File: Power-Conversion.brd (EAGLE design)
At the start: 160 x 100 mm, 25 parts, among them Q1 SUM90P10-19L, U7 LM2678

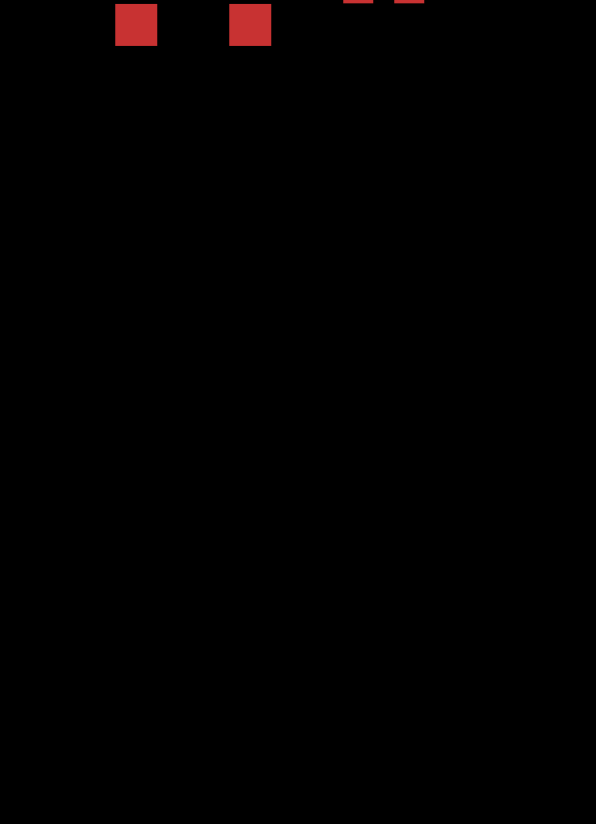
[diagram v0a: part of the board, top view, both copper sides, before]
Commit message: added current sense
added current sense and support things
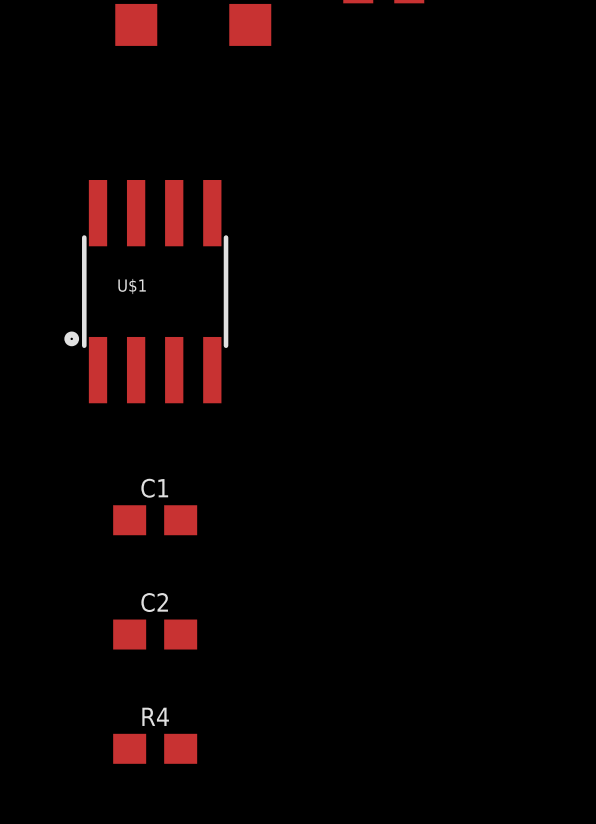
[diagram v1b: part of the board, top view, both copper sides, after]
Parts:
- added C1: .1uF, SparkFun-Capacitors:0603
- added C2: .01uF, SparkFun-Capacitors:0603
- added R4: 10k, SparkFun-Resistors:0603
- added U$1: ACS712, SparkFun-Sensors:SO08
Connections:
- new net +48_SNS: U$1.3, U$1.4
- new net 48_I_ANALOG: C2.2, R4.2, U$1.7
- net +48V: now also U$1.1, U$1.2
- net +5V: now also C1.2, U$1.8
- net GND: now also C1.1, C2.1, R4.1, U$1.5, U$1.6
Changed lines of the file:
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@@
 <attribute name="PARTNO" value="SUM90P10-19L-E3CT-ND" x="-55.88" y="-27.94" size="1.778" layer="27" display="off"/>
+</element>
+<element name="U$1" library="SparkFun-Sensors" package="SO08" value="ACS712" x="-49.53" y="-57.15">
+<attribute name="PROD_ID" value="IC-08964" x="-55.88" y="-44.45" size="1.778" layer="27" display="off"/>
+</element>
+<element name="C1" library="SparkFun-Capacitors" package="0603" value=".1uF" x="-49.53" y="-64.77">
+<attribute name="PROD_ID" value="CAP-08280" x="-55.88" y="-53.34" size="1.778" layer="27" display="off"/>
+</element>
+<element name="C2" library="SparkFun-Capacitors" package="0603" value=".01uF" x="-49.53" y="-68.58">
+<attribute name="PROD_ID" value="CAP-08280" x="-55.88" y="-57.15" size="1.778" layer="27" display="off"/>
+</element>
+<element name="R4" library="SparkFun-Resistors" package="0603" value="10k" x="-49.53" y="-72.39">
+<attribute name="PROD_ID" value="RES-00824" x="-55.88" y="-60.96" size="1.778" layer="27" display="off"/>
 </element>
 </elements>
@@
 <contactref element="LED3" pad="C"/>
 <contactref element="LED4" pad="C"/>
-<wire x1="-26.67" y1="59.17" x2="-22.86" y2="59.17" width="0" layer="19" extent="1-1"/>
-<wire x1="-15.83" y1="46.99" x2="-22.86" y2="59.17" width="0" layer="19" extent="1-1"/>
-<wire x1="-15.83" y1="40.64" x2="-15.83" y2="46.99" width="0" layer="19" extent="1-1"/>
-<wire x1="-15.83" y1="34.29" x2="-15.83" y2="40.64" width="0" layer="19" extent="1-1"/>
-<wire x1="-27.26" y1="40.64" x2="-15.83" y2="40.64" width="0" layer="19" extent="1-1"/>
-<wire x1="-27.26" y1="34.29" x2="-27.26" y2="40.64" width="0" layer="19" extent="1-1"/>
-<wire x1="-25.13" y1="26.415" x2="-27.26" y2="34.29" width="0" layer="19" extent="1-1"/>
-<wire x1="-25.13" y1="21.845" x2="-25.13" y2="26.415" width="0" layer="19" extent="1-1"/>
+<contactref element="U$1" pad="5"/>
+<contactref element="U$1" pad="6"/>
+<contactref element="C1" pad="1"/>
+<contactref element="C2" pad="1"/>
+<contactref element="R4" pad="1"/>
+<wire x1="-50.38" y1="-68.58" x2="-50.38" y2="-72.39" width="0" layer="19" extent="1-1"/>
+<wire x1="-50.38" y1="-64.77" x2="-50.38" y2="-68.58" width="0" layer="19" extent="1-1"/>
+<wire x1="-48.895" y1="-54.5338" x2="-50.38" y2="-64.77" width="0" layer="19" extent="1-1"/>
+<wire x1="-47.625" y1="-54.5338" x2="-48.895" y2="-54.5338" width="0" layer="19" extent="1-1"/>
+<wire x1="-35.56" y1="6.35" x2="-47.625" y2="-54.5338" width="0" layer="19" extent="1-1"/>
+<wire x1="-27.2288" y1="6.35" x2="-35.56" y2="6.35" width="0" layer="19" extent="1-1"/>
+<wire x1="-25.13" y1="21.845" x2="-27.2288" y2="6.35" width="0" layer="19" extent="1-1"/>
+<wire x1="-25.13" y1="26.415" x2="-25.13" y2="21.845" width="0" layer="19" extent="1-1"/>
+<wire x1="-27.26" y1="34.29" x2="-25.13" y2="26.415" width="0" layer="19" extent="1-1"/>
+<wire x1="-27.26" y1="40.64" x2="-27.26" y2="34.29" width="0" layer="19" extent="1-1"/>
 <wire x1="-35.98" y1="46.99" x2="-27.26" y2="40.64" width="0" layer="19" extent="1-1"/>
 <wire x1="-38.69" y1="40.64" x2="-35.98" y2="46.99" width="0" layer="19" extent="1-1"/>
 <wire x1="-38.69" y1="34.29" x2="-38.69" y2="40.64" width="0" layer="19" extent="1-1"/>
-<wire x1="-27.2288" y1="6.35" x2="-25.13" y2="21.845" width="0" layer="19" extent="1-1"/>
-<wire x1="-35.56" y1="6.35" x2="-27.2288" y2="6.35" width="0" layer="19" extent="1-1"/>
+<wire x1="-15.83" y1="40.64" x2="-27.26" y2="40.64" width="0" layer="19" extent="1-1"/>
+<wire x1="-15.83" y1="46.99" x2="-15.83" y2="40.64" width="0" layer="19" extent="1-1"/>
+<wire x1="-15.83" y1="34.29" x2="-15.83" y2="40.64" width="0" layer="19" extent="1-1"/>
+<wire x1="-22.86" y1="59.17" x2="-15.83" y2="46.99" width="0" layer="19" extent="1-1"/>
+<wire x1="-26.67" y1="59.17" x2="-22.86" y2="59.17" width="0" layer="19" extent="1-1"/>
 </signal>
 <signal name="ONOFF">
@@
 <contactref element="C10" pad="+"/>
 <contactref element="R11" pad="2"/>
-<wire x1="-19.05" y1="4.66" x2="-27.2288" y2="8.89" width="0" layer="19" extent="1-1"/>
+<contactref element="U$1" pad="8"/>
+<contactref element="C1" pad="2"/>
+<wire x1="-51.435" y1="-54.5338" x2="-48.68" y2="-64.77" width="0" layer="19" extent="1-1"/>
+<wire x1="0" y1="-25.4" x2="-51.435" y2="-54.5338" width="0" layer="19" extent="1-1"/>
+<wire x1="-19.05" y1="4.66" x2="0" y2="-25.4" width="0" layer="19" extent="1-1"/>
+<wire x1="-27.2288" y1="8.89" x2="-19.05" y2="4.66" width="0" layer="19" extent="1-1"/>
 <wire x1="-22.27" y1="34.29" x2="-27.2288" y2="8.89" width="0" layer="19" extent="1-1"/>
 <wire x1="-33.7" y1="34.29" x2="-22.27" y2="34.29" width="0" layer="19" extent="1-1"/>
 <wire x1="-45.13" y1="34.29" x2="-33.7" y2="34.29" width="0" layer="19" extent="1-1"/>
-<wire x1="0" y1="-25.4" x2="-45.13" y2="34.29" width="0" layer="19" extent="1-1"/>
 </signal>
 <signal name="N$25">
@@
 <contactref element="D1" pad="C"/>
 <contactref element="Q1" pad="2"/>
+<contactref element="U$1" pad="1"/>
+<contactref element="U$1" pad="2"/>
+<wire x1="-50.165" y1="-59.7662" x2="-51.435" y2="-59.7662" width="0" layer="19" extent="1-1"/>
+<wire x1="-50.16" y1="-48.26" x2="-50.165" y2="-59.7662" width="0" layer="19" extent="1-1"/>
 <wire x1="-44.45" y1="-38.35" x2="-50.16" y2="-48.26" width="0" layer="19" extent="1-1"/>
 <wire x1="-48.26" y1="53.17" x2="-44.45" y2="-38.35" width="0" layer="19" extent="1-1"/>
@@
 <contactref element="Q1" pad="3"/>
 </signal>
+<signal name="+48_SNS">
+<contactref element="U$1" pad="3"/>
+<contactref element="U$1" pad="4"/>
+<wire x1="-47.625" y1="-59.7662" x2="-48.895" y2="-59.7662" width="0" layer="19" extent="1-1"/>
+</signal>
+<signal name="48_I_ANALOG">
+<contactref element="U$1" pad="7"/>
+<contactref element="C2" pad="2"/>
+<contactref element="R4" pad="2"/>
+<wire x1="-48.68" y1="-68.58" x2="-48.68" y2="-72.39" width="0" layer="19" extent="1-1"/>
+<wire x1="-50.165" y1="-54.5338" x2="-48.68" y2="-68.58" width="0" layer="19" extent="1-1"/>
+</signal>
 </signals>

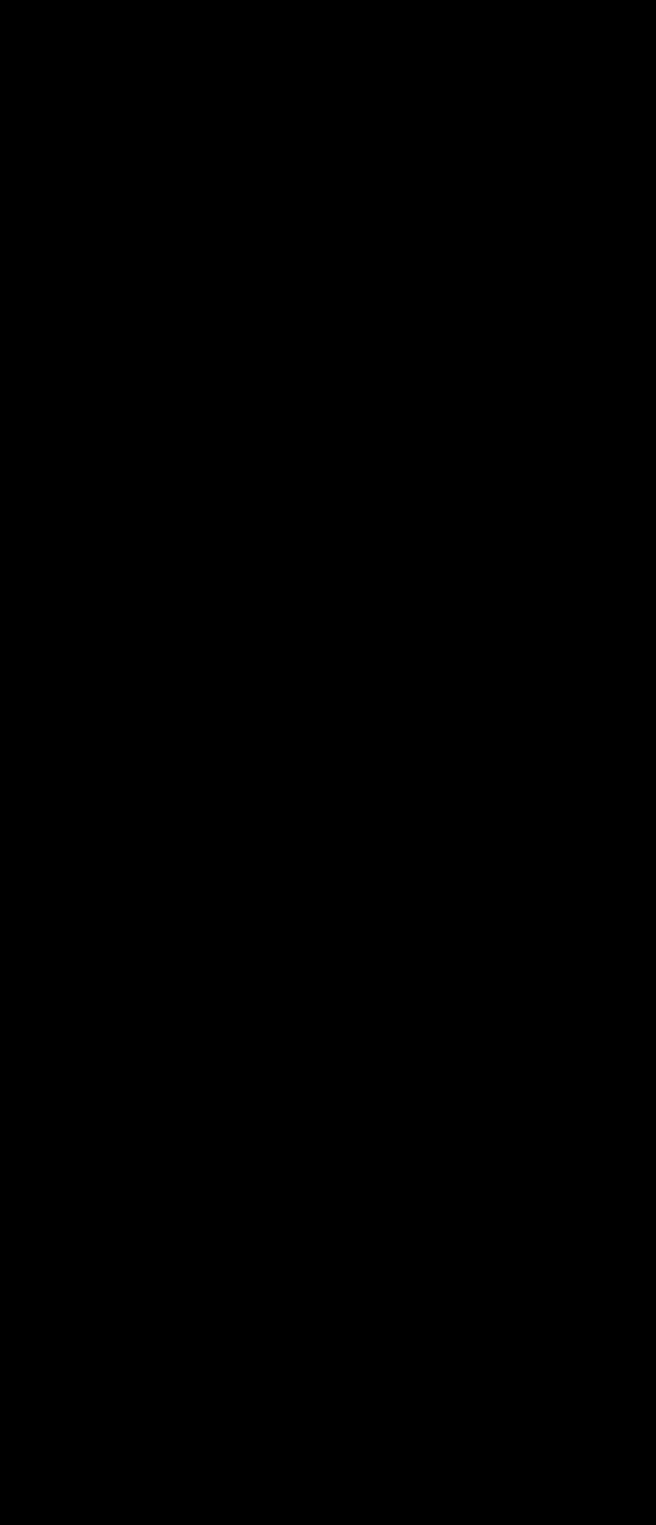
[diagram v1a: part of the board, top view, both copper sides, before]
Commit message: Added voltage connectors
added the voltage connectors
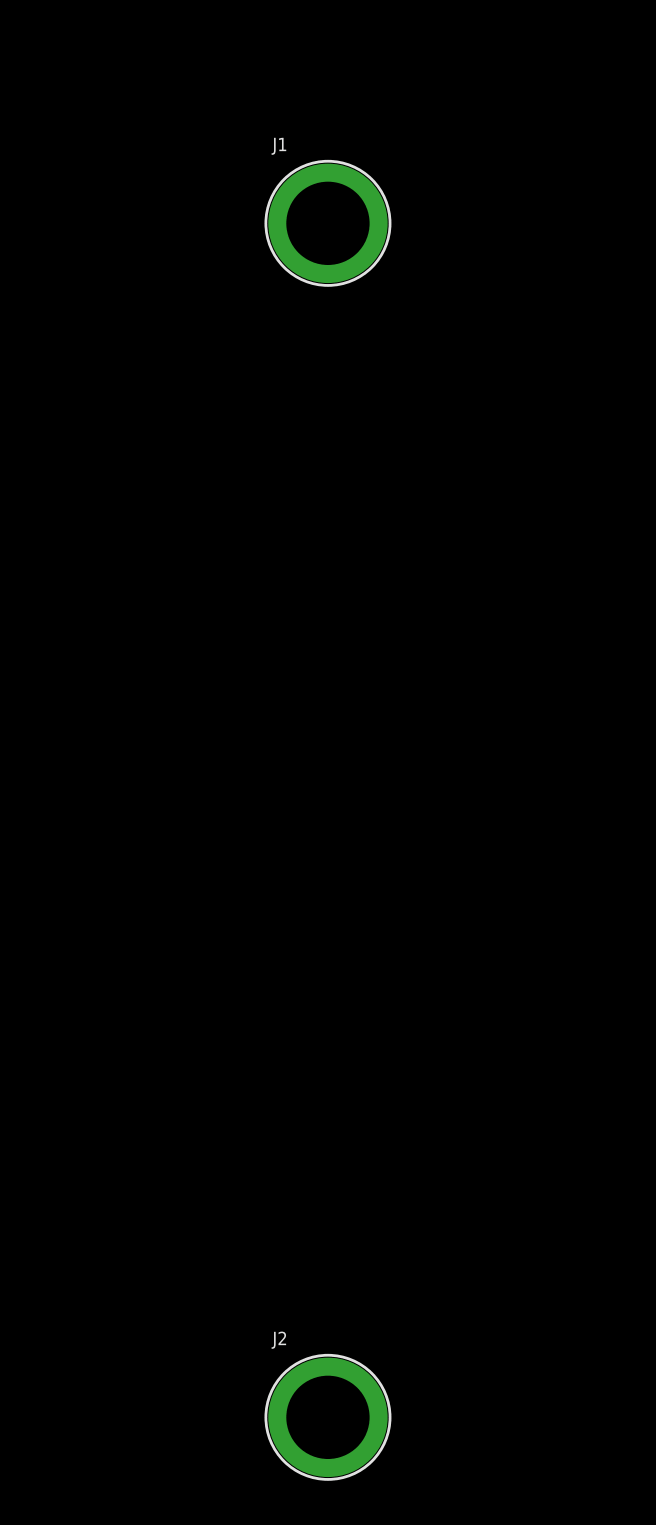
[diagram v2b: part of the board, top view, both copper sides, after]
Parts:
- added J1, J2: (no value), SparkFun-Connectors:BANANA_CONN
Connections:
- net +48V_RAW: now also J1.P$1
- net 48V_GND: now also J2.P$1
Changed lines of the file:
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@@
 <attribute name="PROD_ID" value="RES-00824" x="-55.88" y="-60.96" size="1.778" layer="27" display="off"/>
 </element>
+<element name="J1" library="SparkFun-Connectors" package="BANANA_CONN" value="" x="-25.4" y="-101.6"/>
+<element name="J2" library="SparkFun-Connectors" package="BANANA_CONN" value="" x="-25.4" y="-156.21"/>
 </elements>
 <signals>
@@
 <contactref element="R1" pad="1"/>
 <contactref element="R3" pad="1"/>
+<contactref element="J2" pad="P$1"/>
+<wire x1="-42.76" y1="-46.99" x2="-25.4" y2="-156.21" width="0" layer="19" extent="1-1"/>
 <wire x1="-15.5" y1="21.36" x2="-42.76" y2="-46.99" width="0" layer="19" extent="1-1"/>
 <wire x1="-45.4" y1="51.07" x2="-15.5" y2="21.36" width="0" layer="19" extent="1-1"/>
@@
 <signal name="+48V_RAW">
 <contactref element="Q1" pad="3"/>
+<contactref element="J1" pad="P$1"/>
+<wire x1="-46.99" y1="-28.25" x2="-25.4" y2="-101.6" width="0" layer="19" extent="1-1"/>
 </signal>
 <signal name="+48_SNS">

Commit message: Started Board layout
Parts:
- added U$11, U$12, U$17: POWER_BRICK_CONNECTORS(2X15), MotherBoardParts2:POWER_BRICK_CONNECTORS(2X15)
- added U$13, U$14, U$15: POWER_BRICK_CONNECTORS(2X6), MotherBoardParts2:POWER_BRICK_CONNECTORS(2X6)
- added U$2: SAMTEC-10, SAMTEC-10:POWER-CONNECTOR
- added U$3, U$8: POWER-BRICK-CONNECTOR, MotherboardParts:POWER-BRICK-CONNECTOR
- moved J2 238.8 mm to (-27.9, 82.5)
- moved J1 184.2 mm to (-21.6, 82.5)
- moved R4 167.6 mm to (-50.8, 95.2)
- moved C2 163.8 mm to (-47.0, 95.2)
- moved C1 160.1 mm to (-43.2, 95.2)
- moved R3 145.1 mm to (-20.3, 96.5)
- moved U$1 143.8 mm to (-15.2, 82.5)
- moved D1 139.1 mm to (-62.2, 90.2)
- moved R10 123.2 mm to (-68.6, 90.2)
- moved R11 122.9 mm to (-16.5, 96.5)
- moved U$10 101.9 mm to (68.6, 62.2)
- moved U7 63.6 mm to (-33.0, 69.8)
- moved U$7 58.4 mm to (24.1, 67.3)
- moved C14 55.1 mm to (-53.3, 90.2)
- moved U$9 53.6 mm to (-61.0, 67.3)
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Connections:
- new net +48_RAW: J1.P$1
- new net 12V: U$2.P$5, U$2.P$7, U$2.P$9, U$3.P$27, U$3.P$28, U$3.P$29, U$3.P$30, U$3.P$31, U$3.P$32, U$3.P$33, U$3.P$34, U$3.P$35, U$3.P$36, U$3.P$37, U$3.P$38, U$3.P$39, U$3.P$40, U$3.P$41, U$3.P$42, U$3.P$43, U$3.P$44, U$3.P$45, U$3.P$46, U$3.P$47, U$3.P$48, U$3.P$49, U$3.P$50, U$8.P$1, U$8.P$10, U$8.P$11, U$8.P$12, U$8.P$13, U$8.P$14, U$8.P$15, U$8.P$16, U$8.P$17, U$8.P$18, U$8.P$19, U$8.P$2, U$8.P$20, U$8.P$21, U$8.P$22, U$8.P$23, U$8.P$24, U$8.P$25, U$8.P$26, U$8.P$3, U$8.P$4, U$8.P$5, U$8.P$6, U$8.P$7, U$8.P$8, U$8.P$9
- new net 48_GND: J2.P$1
- new net ON/OFF: U$13.P$11, U$14.P$11, U$15.P$11
- new net SCL: U$13.P$12, U$14.P$12, U$15.P$12, U$2.P$1
- new net SDA: U$13.P$6, U$14.P$6, U$15.P$6, U$2.P$2
- new net VCC: U$13.P$1, U$13.P$2, U$13.P$7, U$13.P$8, U$14.P$1, U$14.P$2, U$14.P$7, U$14.P$8, U$15.P$1, U$15.P$2, U$15.P$7, U$15.P$8
- net +12V: now also U$11.P$1, U$11.P$16, U$11.P$17, U$11.P$18, U$11.P$19, U$11.P$2, U$11.P$20, U$11.P$21, U$11.P$22, U$11.P$3, U$11.P$4, U$11.P$5, U$11.P$6, U$11.P$7, U$12.P$1, U$12.P$16, U$12.P$17, U$12.P$18, U$12.P$19, U$12.P$2, U$12.P$20, U$12.P$21, U$12.P$22, U$12.P$3, U$12.P$4, U$12.P$5, U$12.P$6, U$12.P$7, U$17.P$1, U$17.P$16, U$17.P$17, U$17.P$18, U$17.P$19, U$17.P$2, U$17.P$20, U$17.P$21, U$17.P$22, U$17.P$3, U$17.P$4, U$17.P$5, U$17.P$6, U$17.P$7
- net +48V_RAW: no longer J1.P$1
- net 48V_GND: now also U$13.P$10, U$13.P$3, U$13.P$4, U$13.P$9, U$14.P$10, U$14.P$3, U$14.P$4, U$14.P$9, U$15.P$10, U$15.P$3, U$15.P$4, U$15.P$9; no longer J2.P$1
- net GND: now also U$11.P$10, U$11.P$11, U$11.P$12, U$11.P$13, U$11.P$14, U$11.P$15, U$11.P$24, U$11.P$25, U$11.P$26, U$11.P$27, U$11.P$28, U$11.P$29, U$11.P$30, U$11.P$9, U$12.P$10, U$12.P$11, U$12.P$12, U$12.P$13, U$12.P$14, U$12.P$15, U$12.P$24, U$12.P$25, U$12.P$26, U$12.P$27, U$12.P$28, U$12.P$29, U$12.P$30, U$12.P$9, U$13.P$5, U$14.P$5, U$15.P$5, U$17.P$10, U$17.P$11, U$17.P$12, U$17.P$13, U$17.P$14, U$17.P$15, U$17.P$24, U$17.P$25, U$17.P$26, U$17.P$27, U$17.P$28, U$17.P$29, U$17.P$30, U$17.P$9, U$2.P$10, U$2.P$6, U$2.P$8, U$3.P$1, U$3.P$10, U$3.P$11, U$3.P$12, U$3.P$13, U$3.P$14, U$3.P$15, U$3.P$16, U$3.P$17, U$3.P$18, U$3.P$19, U$3.P$2, U$3.P$20, U$3.P$21, U$3.P$22, U$3.P$23, U$3.P$24, U$3.P$25, U$3.P$26, U$3.P$3, U$3.P$4, U$3.P$5, U$3.P$6, U$3.P$7, U$3.P$8, U$3.P$9, U$8.P$27, U$8.P$28, U$8.P$29, U$8.P$30, U$8.P$31, U$8.P$32, U$8.P$33, U$8.P$34, U$8.P$35, U$8.P$36, U$8.P$37, U$8.P$38, U$8.P$39, U$8.P$40, U$8.P$41, U$8.P$42, U$8.P$43, U$8.P$44, U$8.P$45, U$8.P$46, U$8.P$47, U$8.P$48, U$8.P$49, U$8.P$50
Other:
- board size 160 x 100 mm -> 100 x 80 mm

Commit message: Started Board Layout
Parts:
- removed U$2: SAMTEC-10, SAMTEC-10:POWER-CONNECTOR
- added U$16: POWER_BRICK_CONNECTORS(2X6), MotherBoardParts2:POWER_BRICK_CONNECTORS(2X6)
- moved U$15 252.6 mm to (226.1, 15.2), turned to 90 degrees
- moved U$14 198.5 mm to (175.3, 15.2), turned to 90 degrees
- moved U$12 167.4 mm to (124.5, 81.3), turned to 90 degrees
- moved U$11 165.7 mm to (213.4, 82.5)
- moved U$17 156.4 mm to (174.0, 82.5)
- moved R10 139.0 mm to (50.8, 19.1)
- moved D1 126.5 mm to (43.2, 20.3)
- moved R2 121.5 mm to (30.5, 26.7)
- moved C10 119.6 mm to (57.1, 57.1)
- moved R1 119.0 mm to (10.2, 3.81)
- moved LED3 118.8 mm to (45.7, 38.1)
- moved LED4 118.5 mm to (39.4, 34.3)
- moved U$4 117.8 mm to (47.0, 7.62)
- moved U$3 116.9 mm to (205.7, 48.3), turned to 90 degrees
- moved C14 113.4 mm to (57.1, 64.8)
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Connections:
- net 12V: now also U$16.P$1, U$16.P$2, U$16.P$3; no longer U$2.P$5, U$2.P$7, U$2.P$9
- net 48_I_ANALOG: now also U$16.P$5
- net GND: now also U$16.P$7, U$16.P$8, U$16.P$9; no longer U$2.P$10, U$2.P$6, U$2.P$8
- net SCL: now also U$16.P$12; no longer U$2.P$1
- net SDA: now also U$16.P$6; no longer U$2.P$2
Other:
- board size 100 x 80 mm -> 252.4 x 86.3 mm

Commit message: Fix Board Layout
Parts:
- moved U$15 68.6 mm to (157.5, 16.5)
- moved U$13 58.4 mm to (193.0, 15.2)
- moved C9 56.7 mm to (9.14, 49.8), turned to 180 degrees
- moved R10 53.4 mm to (23.6, 65.0), turned to 90 degrees
- moved C8 50.7 mm to (9.14, 56.1), turned to 180 degrees
- moved C10 48.3 mm to (9.14, 62.5), turned to 180 degrees
- moved R11 47.4 mm to (19.8, 65.0), turned to 90 degrees
- moved C1 46.5 mm to (4.06, 42.2), turned to 270 degrees
- moved U$14 43.2 mm to (132.1, 15.2)
- moved U$8 36.9 mm to (105.4, 47.0)
- moved J2 33.4 mm to (5.08, 3.81)
- moved LED4 33.1 mm to (19.8, 61.0), turned to 180 degrees
- moved J1 32.2 mm to (5.08, 11.4)
- moved LED3 31.8 mm to (23.6, 61.0), turned to 180 degrees
- moved U$7 30.7 mm to (40.6, 5.08), turned to 90 degrees
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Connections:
- removed net +48_RAW: J1.P$1
- removed net 48_GND: J2.P$1
- net +48V_RAW: now also J1.P$1
- net 48V_GND: now also J2.P$1
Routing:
- net GND: track 0.00 -> 23.4 mm
- net 48V_GND: track 0.00 -> 6.60 mm, vias 0 -> 2
- added copper zone on layer 1, net +12V
- added copper zone on layer 1, net +48V_RAW
- added copper zone on layer 1, net +5V
- added copper zone on layer 16, net 48V_GND
- added copper zone on layer 1, net GND

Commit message: Routed Board
Added Diodes
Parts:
- added U$18, U$19, U$2: DIODE, diode:DIODE
- moved C13 44.6 mm to (41.1, 45.7)
- moved C11 34.5 mm to (34.0, 45.7)
- moved C8 33.0 mm to (42.2, 57.4), turned to 270 degrees
- moved R10 32.0 mm to (46.7, 42.9), turned to 270 degrees
- moved C3 31.3 mm to (8.38, 58.4), turned to 270 degrees
- moved C14 29.6 mm to (20.3, 45.7)
- moved C12 28.7 mm to (27.2, 45.7)
- moved LED4 27.9 mm to (46.7, 53.6)
- moved R11 27.4 mm to (46.7, 59.9)
- moved C10 26.9 mm to (35.6, 57.4), turned to 270 degrees
- moved LED3 26.0 mm to (46.7, 49.0), turned to 0 degrees
- moved U7 25.5 mm to (19.3, 57.7)
- moved U$10 24.6 mm to (37.1, 70.6), turned to 90 degrees
- moved U$9 23.8 mm to (21.6, 66.5)
- moved C9 21.2 mm to (29.0, 57.4), turned to 270 degrees
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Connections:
- removed net +48_SNS: U$1.3, U$1.4
- removed net VCC: U$13.P$1, U$13.P$2, U$13.P$7, U$13.P$8, U$14.P$1, U$14.P$2, U$14.P$7, U$14.P$8, U$15.P$1, U$15.P$2, U$15.P$7, U$15.P$8
- new net +12V_1: U$17.P$1, U$17.P$16, U$17.P$17, U$17.P$18, U$17.P$19, U$17.P$2, U$17.P$20, U$17.P$21, U$17.P$22, U$17.P$3, U$17.P$4, U$17.P$5, U$17.P$6, U$17.P$7, U$2.IN1, U$2.IN2
- new net +12V_2: U$11.P$1, U$11.P$16, U$11.P$17, U$11.P$18, U$11.P$19, U$11.P$2, U$11.P$20, U$11.P$21, U$11.P$22, U$11.P$3, U$11.P$4, U$11.P$5, U$11.P$6, U$11.P$7, U$18.IN1, U$18.IN2
- new net +12V_3: U$12.P$1, U$12.P$16, U$12.P$17, U$12.P$18, U$12.P$19, U$12.P$2, U$12.P$20, U$12.P$21, U$12.P$22, U$12.P$3, U$12.P$4, U$12.P$5, U$12.P$6, U$12.P$7, U$19.IN1, U$19.IN2
- new net +48V_SNS: U$1.3, U$1.4, U$13.P$1, U$13.P$2, U$13.P$7, U$13.P$8, U$14.P$1, U$14.P$2, U$14.P$7, U$14.P$8, U$15.P$1, U$15.P$2, U$15.P$7, U$15.P$8
- net +12V: now also U$18.OUT, U$19.OUT, U$2.OUT; no longer U$11.P$1, U$11.P$16, U$11.P$17, U$11.P$18, U$11.P$19, U$11.P$2, U$11.P$20, U$11.P$21, U$11.P$22, U$11.P$3, U$11.P$4, U$11.P$5, U$11.P$6, U$11.P$7, U$12.P$1, U$12.P$16, U$12.P$17, U$12.P$18, U$12.P$19, U$12.P$2, U$12.P$20, U$12.P$21, U$12.P$22, U$12.P$3, U$12.P$4, U$12.P$5, U$12.P$6, U$12.P$7, U$17.P$1, U$17.P$16, U$17.P$17, U$17.P$18, U$17.P$19, U$17.P$2, U$17.P$20, U$17.P$21, U$17.P$22, U$17.P$3, U$17.P$4, U$17.P$5, U$17.P$6, U$17.P$7
- net 12V: now also U$8.P$27, U$8.P$28, U$8.P$29, U$8.P$30, U$8.P$31, U$8.P$32, U$8.P$33, U$8.P$34, U$8.P$35, U$8.P$36, U$8.P$37, U$8.P$38, U$8.P$39, U$8.P$40, U$8.P$41, U$8.P$42, U$8.P$43, U$8.P$44, U$8.P$45, U$8.P$46, U$8.P$47, U$8.P$48, U$8.P$49, U$8.P$50; no longer U$3.P$27, U$3.P$28, U$3.P$29, U$3.P$30, U$3.P$31, U$3.P$32, U$3.P$33, U$3.P$34, U$3.P$35, U$3.P$36, U$3.P$37, U$3.P$38, U$3.P$39, U$3.P$40, U$3.P$41, U$3.P$42, U$3.P$43, U$3.P$44, U$3.P$45, U$3.P$46, U$3.P$47, U$3.P$48, U$3.P$49, U$3.P$50
- net GND: now also U$3.P$27, U$3.P$28, U$3.P$29, U$3.P$30, U$3.P$31, U$3.P$32, U$3.P$33, U$3.P$34, U$3.P$35, U$3.P$36, U$3.P$37, U$3.P$38, U$3.P$39, U$3.P$40, U$3.P$41, U$3.P$42, U$3.P$43, U$3.P$44, U$3.P$45, U$3.P$46, U$3.P$47, U$3.P$48, U$3.P$49, U$3.P$50; no longer U$8.P$27, U$8.P$28, U$8.P$29, U$8.P$30, U$8.P$31, U$8.P$32, U$8.P$33, U$8.P$34, U$8.P$35, U$8.P$36, U$8.P$37, U$8.P$38, U$8.P$39, U$8.P$40, U$8.P$41, U$8.P$42, U$8.P$43, U$8.P$44, U$8.P$45, U$8.P$46, U$8.P$47, U$8.P$48, U$8.P$49, U$8.P$50
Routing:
- net +5V: track 0.00 -> 50.8 mm, vias 0 -> 2
- net +12V: track 0.00 -> 47.3 mm, vias 0 -> 2
- net GND: track 23.4 -> 53.8 mm
- net N$36: track 0.00 -> 26.2 mm
- net N$10: track 0.00 -> 23.5 mm
- net ONOFF: track 0.00 -> 10.6 mm
- net N$5: track 0.00 -> 9.96 mm
- net N$25: track 0.00 -> 6.93 mm
- net 48_I_ANALOG: track 0.00 -> 6.62 mm
- net N$40: track 0.00 -> 4.75 mm
- net N$39: track 0.00 -> 4.50 mm
- net 48V_GND: track 6.60 -> 9.66 mm
- net N$9: track 0.00 -> 2.20 mm
- added copper zone on layer 1, net +48V
